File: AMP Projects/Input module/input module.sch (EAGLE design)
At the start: 16 parts, among them IC1 OPAMP-DUALU

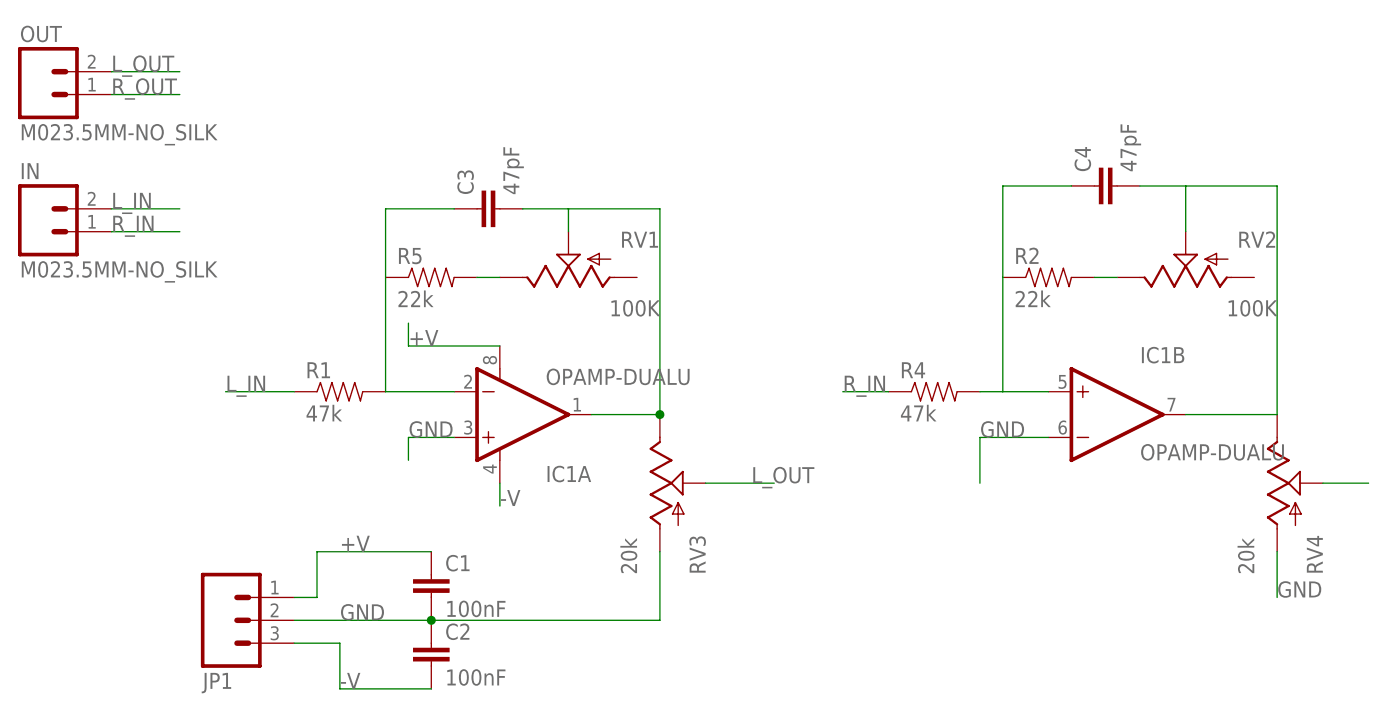
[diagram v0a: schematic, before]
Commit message: Fixed incorrect usage of op-amp on pre-amplifier.
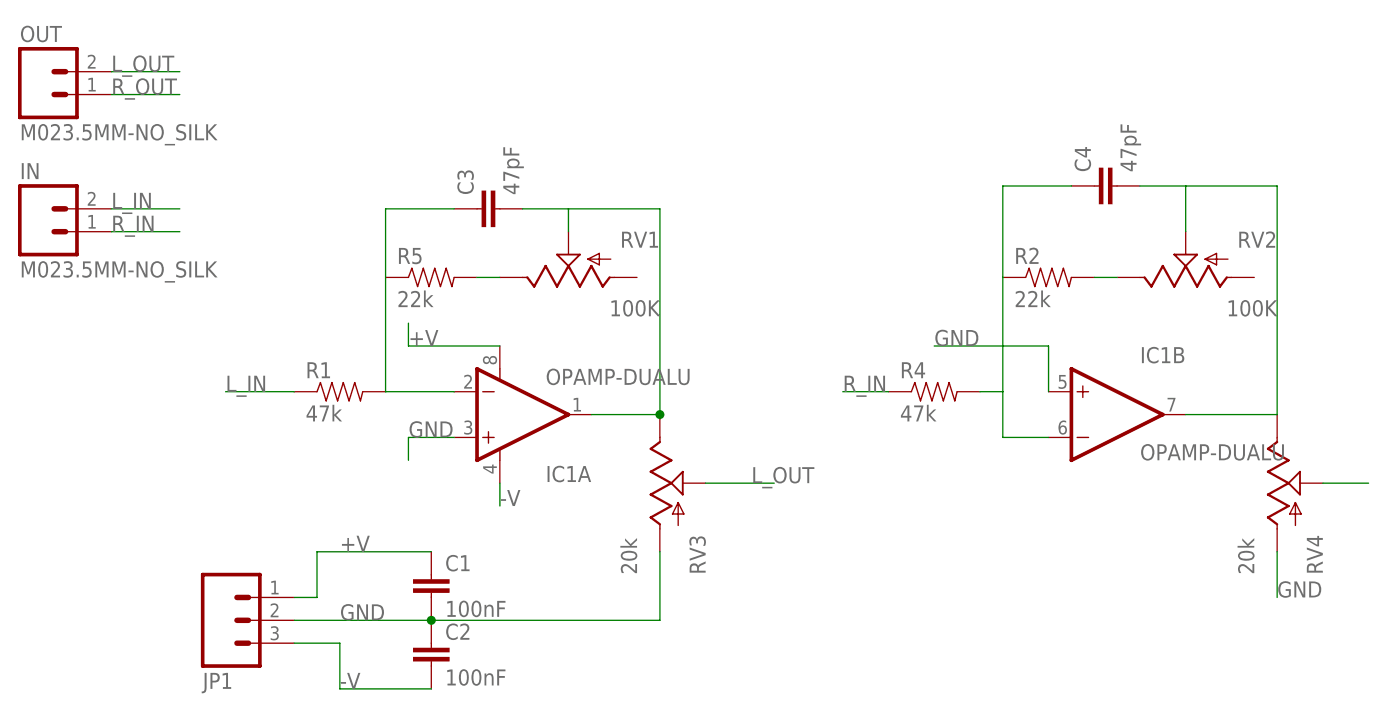
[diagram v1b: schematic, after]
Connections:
- net GND: now also IC1B.+IN; no longer IC1B.-IN
- net N$3: now also IC1B.-IN; no longer IC1B.+IN
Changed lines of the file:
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@@
 <?xml version="1.0" encoding="utf-8"?>
 <!DOCTYPE eagle SYSTEM "eagle.dtd">
-<eagle version="6.5.0">
+<eagle version="7.7.0">
 <drawing>
 <settings>
@@
 </segment>
 <segment>
-<pinref part="IC1" gate="B" pin="-IN"/>
-<wire x1="83.82" y1="55.88" x2="76.2" y2="55.88" width="0.1524" layer="91"/>
-<wire x1="76.2" y1="55.88" x2="76.2" y2="50.8" width="0.1524" layer="91"/>
-<label x="76.2" y="55.88" size="1.778" layer="95"/>
+<label x="71.12" y="66.04" size="1.778" layer="95"/>
+<wire x1="71.12" y1="66.04" x2="83.82" y2="66.04" width="0.1524" layer="91"/>
+<pinref part="IC1" gate="B" pin="+IN"/>
+<wire x1="83.82" y1="66.04" x2="83.82" y2="60.96" width="0.1524" layer="91"/>
 </segment>
 </net>
@@
 <wire x1="86.36" y1="83.82" x2="78.74" y2="83.82" width="0.1524" layer="91"/>
 <wire x1="78.74" y1="83.82" x2="78.74" y2="73.66" width="0.1524" layer="91"/>
-<wire x1="78.74" y1="73.66" x2="78.74" y2="60.96" width="0.1524" layer="91"/>
 <pinref part="R4" gate="G$1" pin="2"/>
 <wire x1="76.2" y1="60.96" x2="78.74" y2="60.96" width="0.1524" layer="91"/>
-<pinref part="IC1" gate="B" pin="+IN"/>
-<wire x1="78.74" y1="60.96" x2="83.82" y2="60.96" width="0.1524" layer="91"/>
-</segment>
-</net>
+<wire x1="78.74" y1="73.66" x2="78.74" y2="60.96" width="0.1524" layer="91"/>
+<wire x1="78.74" y1="60.96" x2="78.74" y2="55.88" width="0.1524" layer="91"/>
+<pinref part="IC1" gate="B" pin="-IN"/>
+<wire x1="78.74" y1="55.88" x2="83.82" y2="55.88" width="0.1524" layer="91"/>
+</segment>
+</net>
